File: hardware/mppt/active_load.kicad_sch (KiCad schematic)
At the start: 10 parts, among them Q601 Q_NMOS_GSD

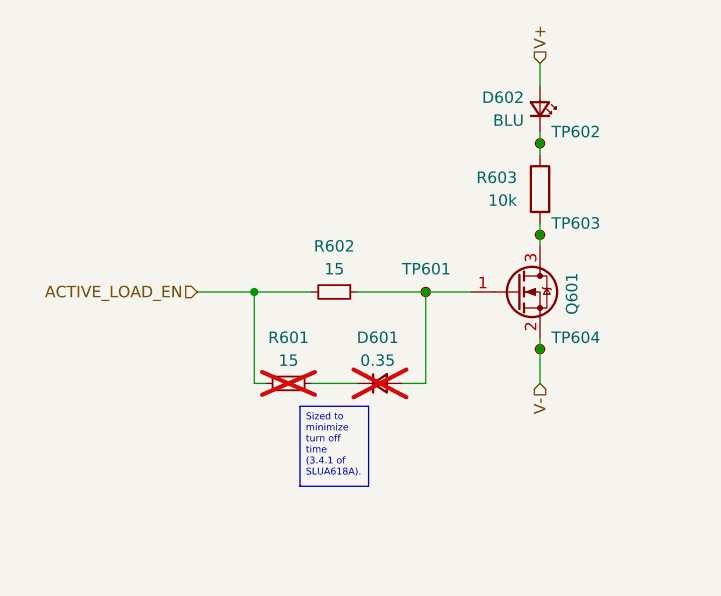
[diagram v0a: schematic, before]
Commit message: run through mppt sch, going through bom
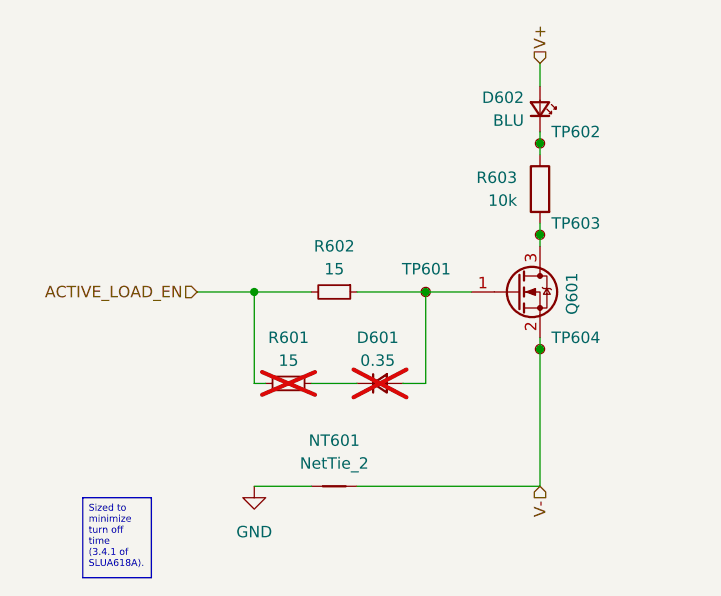
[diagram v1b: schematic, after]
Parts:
- added NT601: NetTie_2, symbol Device:NetTie_2
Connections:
- net V-: now also NT601.2
- new net GND: NT601.1

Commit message: update final missing pieces for sch, moving to bom pop
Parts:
- removed Q601: Q_NMOS_GSD, Package_TO_SOT_SMD:SOT-23-3, symbol Device:Q_NMOS_GSD
- added Q601: Q_NMOS_GDS, Package_TO_SOT_SMD:SOT-223-3_TabPin2, symbol Device:Q_NMOS_GDS
- D601: symbol Device:D_Small -> Device:D_Schottky_Small
- NT601: footprint (none) -> NetTie:NetTie-2_SMD_Pad2.0mm
- R601, R602: footprint Resistor_SMD:R_0805_2012Metric_Pad1.20x1.40mm_HandSolder -> (none)
- TP601, TP602, TP603, TP604: footprint TestPoint:TestPoint_Keystone_5000-5004_Miniature -> TestPoint:TestPoint_Pad_D1.0mm; Manufacturer Keystone Electronics -> (none); P/N 5000 -> (none)
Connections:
- net V-: now also Q601.3 (S)
- net at D601.2 (A), R602.1, TP601.1: now also Q601.1 (G)
- net at R603.2, TP603.1: now also Q601.2 (D)
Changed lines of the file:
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@@
 			)
 		)
-		(property "Footprint" ""
+		(property "Footprint" "NetTie:NetTie-2_SMD_Pad2.0mm"
 			(at 116.84 123.19 0)
 			(effects
@@
 			)
 		)
-		(property "Datasheet" "~"
+		(property "Datasheet" ""
 			(at 116.84 123.19 0)
 			(effects
@@
 			)
 		)
-		(property "Footprint" "TestPoint:TestPoint_Keystone_5000-5004_Miniature"
+		(property "Footprint" "TestPoint:TestPoint_Pad_D1.0mm"
 			(at 121.92 101.6 0)
 			(effects
@@
 			)
 		)
-		(property "Datasheet" "https://www.keyelco.com/userAssets/file/M65p56.pdf"
+		(property "Datasheet" ""
 			(at 121.92 101.6 0)
 			(effects
@@
 			)
 		)
-		(property "Manufacturer" "Keystone Electronics"
+		(property "Manufacturer" ""
 			(at 127 101.6 0)
 			(effects
@@
 			)
 		)
-		(property "P/N" "5000"
+		(property "P/N" ""
 			(at 127 101.6 0)
 			(effects
@@
 			)
 		)
-		(property "Footprint" "TestPoint:TestPoint_Keystone_5000-5004_Miniature"
+		(property "Footprint" "TestPoint:TestPoint_Pad_D1.0mm"
 			(at 144.78 107.95 0)
 			(effects
@@
 			)
 		)
-		(property "Datasheet" "https://www.keyelco.com/userAssets/file/M65p56.pdf"
+		(property "Datasheet" ""
 			(at 144.78 107.95 0)
 			(effects
@@
 			)
 		)
-		(property "Manufacturer" "Keystone Electronics"
+		(property "Manufacturer" ""
 			(at 139.7 107.95 0)
 			(effects
@@
 			)
 		)
-		(property "P/N" "5000"
+		(property "P/N" ""
 			(at 139.7 107.95 0)
 			(effects
@@
 	)
 	(symbol
-		(lib_id "Device:D_Small")
+		(lib_id "Device:D_Schottky_Small")
 		(at 121.92 111.76 0)
 		(mirror x)
@@
 			)
 		)
-		(property "Datasheet" "https://www.mouser.com/datasheet/2/115/DIOD_S_A0002960396_1-2542090.pdf"
+		(property "Datasheet" "~"
 			(at 121.92 111.76 90)
 			(effects
@@
 			)
 		)
-		(property "Description" "Diode, small symbol"
+		(property "Description" "Schottky diode, small symbol"
 			(at 121.92 111.76 0)
 			(effects
@@
 			)
 		)
-		(property "Footprint" "TestPoint:TestPoint_Keystone_5000-5004_Miniature"
+		(property "Footprint" "TestPoint:TestPoint_Pad_D1.0mm"
 			(at 144.78 85.09 0)
 			(effects
@@
 			)
 		)
-		(property "Datasheet" "https://www.keyelco.com/userAssets/file/M65p56.pdf"
+		(property "Datasheet" ""
 			(at 144.78 85.09 0)
 			(effects
@@
 			)
 		)
-		(property "Manufacturer" "Keystone Electronics"
+		(property "Manufacturer" ""
 			(at 139.7 85.09 0)
 			(effects
@@
 			)
 		)
-		(property "P/N" "5000"
+		(property "P/N" ""
 			(at 139.7 85.09 0)
 			(effects
@@
 			)
 		)
-		(property "Footprint" "TestPoint:TestPoint_Keystone_5000-5004_Miniature"
+		(property "Footprint" "TestPoint:TestPoint_Pad_D1.0mm"
 			(at 144.78 95.25 0)
 			(effects
@@
 			)
 		)
-		(property "Datasheet" "https://www.keyelco.com/userAssets/file/M65p56.pdf"
+		(property "Datasheet" ""
 			(at 144.78 95.25 0)
 			(effects
@@
 			)
 		)
-		(property "Manufacturer" "Keystone Electronics"
+		(property "Manufacturer" ""
 			(at 139.7 95.25 0)
 			(effects
@@
 			)
 		)
-		(property "P/N" "5000"
+		(property "P/N" ""
 			(at 139.7 95.25 0)
 			(effects
@@
 				(path "/83ad0d2f-976b-4ec4-beba-98e6b6988069/1e7e948a-199f-4420-b7b6-1130e9474bfe/a7b76023-5527-427b-b6b3-61ece243dcb4"
 					(reference "TP703")
-					(unit 1)
-				)
-			)
-		)
-	)
-	(symbol
-		(lib_id "Device:Q_NMOS_GSD")
-		(at 137.16 101.6 0)
-		(unit 1)
-		(exclude_from_sim no)
-		(in_bom yes)
-		(on_board yes)
-		(dnp no)
-		(property "Reference" "Q601"
-			(at 143.256 104.14 90)
-			(effects
-				(font
-					(size 1.27 1.27)
-				)
-				(justify left)
-			)
-		)
-		(property "Value" "Q_NMOS_GSD"
-			(at 143.51 102.8699 0)
-			(effects
-				(font
-					(size 1.27 1.27)
-				)
-				(justify left)
-				(hide yes)
-			)
-		)
-		(property "Footprint" "Package_TO_SOT_SMD:SOT-23-3"
-			(at 142.24 99.06 0)
-			(effects
-				(font
-					(size 1.27 1.27)
-				)
-				(hide yes)
-			)
-		)
-		(property "Datasheet" "https://www.mouser.com/datasheet/2/196/Infineon_BSS131_DS_v02_06_en-1226437.pdf"
-			(at 137.16 101.6 0)
-			(effects
-				(font
-					(size 1.27 1.27)
-				)
-				(hide yes)
-			)
-		)
-		(property "Description" "N-MOSFET transistor, gate/source/drain"
-			(at 137.16 101.6 0)
-			(effects
-				(font
-					(size 1.27 1.27)
-				)
-				(hide yes)
-			)
-		)
-		(property "Distributor" ""
-			(at 137.16 101.6 0)
-			(effects
-				(font
-					(size 1.27 1.27)
-				)
-				(hide yes)
-			)
-		)
-		(property "Manufacturer" "Infineon"
-			(at 137.16 101.6 0)
-			(effects
-				(font
-					(size 1.27 1.27)
-				)
-				(hide yes)
-			)
-		)
-		(property "P/N" "BSS131"
-			(at 137.16 101.6 0)
-			(effects
-				(font
-					(size 1.27 1.27)
-				)
-				(hide yes)
-			)
-		)
-		(property "LCSC Part #" ""
-			(at 137.16 101.6 0)
-			(effects
-				(font
-					(size 1.27 1.27)
-				)
-				(hide yes)
-			)
-		)
-		(property "Cost" ""
-			(at 137.16 101.6 0)
-			(effects
-				(font
-					(size 1.27 1.27)
-				)
-				(hide yes)
-			)
-		)
-		(property "Notes" ""
-			(at 137.16 101.6 0)
-			(effects
-				(font
-					(size 1.27 1.27)
-				)
-				(hide yes)
-			)
-		)
-		(property "Sim.Device" ""
-			(at 137.16 101.6 0)
-			(effects
-				(font
-					(size 1.27 1.27)
-				)
-				(hide yes)
-			)
-		)
-		(property "Sim.Pins" ""
-			(at 137.16 101.6 0)
-			(effects
-				(font
-					(size 1.27 1.27)
-				)
-				(hide yes)
-			)
-		)
-		(pin "3"
-		)
-		(pin "1"
-		)
-		(pin "2"
-		)
-		(instances
-			(project "mppt"
-				(path "/83ad0d2f-976b-4ec4-beba-98e6b6988069/1e7e948a-199f-4420-b7b6-1130e9474bfe/3cc71787-1ecf-4ebc-9258-dc128425d892"
-					(reference "Q601")
-					(unit 1)
-				)
-				(path "/83ad0d2f-976b-4ec4-beba-98e6b6988069/1e7e948a-199f-4420-b7b6-1130e9474bfe/a7b76023-5527-427b-b6b3-61ece243dcb4"
-					(reference "Q701")
 					(unit 1)
 				)
@@
 			)
 		)
-		(property "Footprint" "Resistor_SMD:R_0805_2012Metric_Pad1.20x1.40mm_HandSolder"
+		(property "Footprint" ""
 			(at 111.76 111.76 0)
 			(effects
@@
 	)
 	(symbol
+		(lib_id "Device:Q_NMOS_GDS")
+		(at 137.16 101.6 0)
+		(unit 1)
+		(exclude_from_sim no)
+		(in_bom yes)
+		(on_board yes)
+		(dnp no)
+		(fields_autoplaced yes)
+		(property "Reference" "Q601"
+			(at 143.51 100.3299 0)
+			(effects
+				(font
+					(size 1.27 1.27)
+				)
+				(justify left)
+			)
+		)
+		(property "Value" "Q_NMOS_GDS"
+			(at 143.51 102.8699 0)
+			(effects
+				(font
+					(size 1.27 1.27)
+				)
+				(justify left)
+			)
+		)
+		(property "Footprint" "Package_TO_SOT_SMD:SOT-223-3_TabPin2"
+			(at 142.24 99.06 0)
+			(effects
+				(font
+					(size 1.27 1.27)
+				)
+				(hide yes)
+			)
+		)
+		(property "Datasheet" "~"
+			(at 137.16 101.6 0)
+			(effects
+				(font
+					(size 1.27 1.27)
+				)
+				(hide yes)
+			)
+		)
+		(property "Description" "N-MOSFET transistor, gate/drain/source"
+			(at 137.16 101.6 0)
+			(effects
+				(font
+					(size 1.27 1.27)
+				)
+				(hide yes)
+			)
+		)
+		(property "Distributor" ""
+			(at 137.16 101.6 0)
+			(effects
+				(font
+					(size 1.27 1.27)
+				)
+				(hide yes)
+			)
+		)
+		(property "Manufacturer" "Infineon"
+			(at 137.16 101.6 0)
+			(effects
+				(font
+					(size 1.27 1.27)
+				)
+				(hide yes)
+			)
+		)
+		(property "P/N" "BSP297H6327"
+			(at 137.16 101.6 0)
+			(effects
+				(font
+					(size 1.27 1.27)
+				)
+				(hide yes)
+			)
+		)
+		(property "LCSC Part #" ""
+			(at 137.16 101.6 0)
+			(effects
+				(font
+					(size 1.27 1.27)
+				)
+				(hide yes)
+			)
+		)
+		(property "Cost" ""
+			(at 137.16 101.6 0)
+			(effects
+				(font
+					(size 1.27 1.27)
+				)
+				(hide yes)
+			)
+		)
+		(property "Notes" ""
+			(at 137.16 101.6 0)
+			(effects
+				(font
+					(size 1.27 1.27)
+				)
+				(hide yes)
+			)
+		)
+		(pin "3"
+		)
+		(pin "2"
+		)
+		(pin "1"
+		)
+		(instances
+			(project "mppt"
+				(path "/83ad0d2f-976b-4ec4-beba-98e6b6988069/1e7e948a-199f-4420-b7b6-1130e9474bfe/3cc71787-1ecf-4ebc-9258-dc128425d892"
+					(reference "Q601")
+					(unit 1)
+				)
+				(path "/83ad0d2f-976b-4ec4-beba-98e6b6988069/1e7e948a-199f-4420-b7b6-1130e9474bfe/a7b76023-5527-427b-b6b3-61ece243dcb4"
+					(reference "Q701")
+					(unit 1)
+				)
+			)
+		)
+	)
+	(symbol
 		(lib_id "Device:R_Small")
 		(at 116.84 101.6 270)
@@
 			)
 		)
-		(property "Footprint" "Resistor_SMD:R_0805_2012Metric_Pad1.20x1.40mm_HandSolder"
+		(property "Footprint" ""
 			(at 116.84 101.6 0)
 			(effects

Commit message: bom consolidated, starting layout
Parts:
- D601: value 0.35 -> Schottky
- D602: Manufacturer (none) -> Kingbright; P/N (none) -> APT2012QBC/D
- NT601: footprint NetTie:NetTie-2_SMD_Pad2.0mm -> NetTie:NetTie-2_SMD_Pad0.5mm
- R601, R602: footprint (none) -> Resistor_SMD:R_1210_3225Metric_Pad1.30x2.65mm_HandSolder; P/N (none) -> CRCW121015R0FKEA
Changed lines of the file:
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@@
 			)
 		)
-		(property "Footprint" "NetTie:NetTie-2_SMD_Pad2.0mm"
+		(property "Footprint" "NetTie:NetTie-2_SMD_Pad0.5mm"
 			(at 116.84 123.19 0)
 			(effects
@@
 		)
 		(property "Description" "Net tie, 2 pins"
-			(at 116.84 123.19 0)
-			(effects
-				(font
-					(size 1.27 1.27)
-				)
-				(hide yes)
-			)
-		)
-		(property "Sim.Device" ""
-			(at 116.84 123.19 0)
-			(effects
-				(font
-					(size 1.27 1.27)
-				)
-				(hide yes)
-			)
-		)
-		(property "Sim.Pins" ""
 			(at 116.84 123.19 0)
 			(effects
@@
 			)
 		)
-		(property "Sim.Device" ""
-			(at 127 101.6 0)
-			(effects
-				(font
-					(size 1.27 1.27)
-				)
-				(hide yes)
-			)
-		)
-		(property "Sim.Pins" ""
-			(at 127 101.6 0)
-			(effects
-				(font
-					(size 1.27 1.27)
-				)
-				(hide yes)
-			)
-		)
 		(pin "1"
 		)
@@
 			)
 		)
-		(property "Sim.Device" ""
-			(at 139.7 107.95 0)
-			(effects
-				(font
-					(size 1.27 1.27)
-				)
-				(hide yes)
-			)
-		)
-		(property "Sim.Pins" ""
-			(at 139.7 107.95 0)
-			(effects
-				(font
-					(size 1.27 1.27)
-				)
-				(hide yes)
-			)
-		)
 		(pin "1"
 		)
@@
 			)
 		)
-		(property "Value" "0.35"
+		(property "Value" "Schottky"
 			(at 121.666 109.22 0)
 			(effects
@@
 			)
 		)
-		(property "Datasheet" "~"
+		(property "Datasheet" "https://www.mouser.com/datasheet/2/115/DIOD_S_A0002960396_1-2542090.pdf"
 			(at 121.92 111.76 90)
 			(effects
@@
 		(property "Notes" ""
 			(at 121.92 111.76 90)
-			(effects
-				(font
-					(size 1.27 1.27)
-				)
-				(hide yes)
-			)
-		)
-		(property "Sim.Device" ""
-			(at 121.92 111.76 0)
-			(effects
-				(font
-					(size 1.27 1.27)
-				)
-				(hide yes)
-			)
-		)
-		(property "Sim.Pins" ""
-			(at 121.92 111.76 0)
 			(effects
 				(font
@@
 			)
 		)
-		(property "Datasheet" ""
+		(property "Datasheet" "https://www.mouser.com/datasheet/2/216/APT2012QBC_D-226241.pdf"
 			(at 139.7 81.28 90)
 			(effects
@@
 			)
 		)
-		(property "Manufacturer" ""
+		(property "Manufacturer" "Kingbright"
 			(at 139.7 81.28 90)
 			(effects
@@
 			)
 		)
-		(property "P/N" ""
+		(property "P/N" " APT2012QBC/D "
 			(at 139.7 81.28 90)
 			(effects
@@
 		(property "Notes" ""
 			(at 139.7 81.28 90)
-			(effects
-				(font
-					(size 1.27 1.27)
-				)
-				(hide yes)
-			)
-		)
-		(property "Sim.Device" ""
-			(at 139.7 81.28 0)
-			(effects
-				(font
-					(size 1.27 1.27)
-				)
-				(hide yes)
-			)
-		)
-		(property "Sim.Pins" ""
-			(at 139.7 81.28 0)
 			(effects
 				(font
@@
 			)
 		)
-		(property "Sim.Device" ""
-			(at 139.7 85.09 0)
-			(effects
-				(font
-					(size 1.27 1.27)
-				)
-				(hide yes)
-			)
-		)
-		(property "Sim.Pins" ""
-			(at 139.7 85.09 0)
-			(effects
-				(font
-					(size 1.27 1.27)
-				)
-				(hide yes)
-			)
-		)
 		(pin "1"
 		)
@@
 			)
 		)
-		(property "Sim.Device" ""
-			(at 139.7 95.25 0)
-			(effects
-				(font
-					(size 1.27 1.27)
-				)
-				(hide yes)
-			)
-		)
-		(property "Sim.Pins" ""
-			(at 139.7 95.25 0)
-			(effects
-				(font
-					(size 1.27 1.27)
-				)
-				(hide yes)
-			)
-		)
 		(pin "1"
 		)
@@
 			)
 		)
-		(property "Footprint" ""
+		(property "Footprint" "Resistor_SMD:R_1210_3225Metric_Pad1.30x2.65mm_HandSolder"
 			(at 111.76 111.76 0)
 			(effects
@@
 			)
 		)
-		(property "Datasheet" ""
+		(property "Datasheet" "https://www.vishay.com/docs/20035/dcrcwe3.pdf"
 			(at 111.76 111.76 0)
 			(effects
@@
 			)
 		)
-		(property "P/N" ""
-			(at 111.76 111.76 0)
-			(effects
-				(font
-					(size 1.27 1.27)
-				)
-				(hide yes)
-			)
-		)
-		(property "Sim.Device" ""
-			(at 111.76 111.76 0)
-			(effects
-				(font
-					(size 1.27 1.27)
-				)
-				(hide yes)
-			)
-		)
-		(property "Sim.Pins" ""
+		(property "P/N" "CRCW121015R0FKEA "
 			(at 111.76 111.76 0)
 			(effects
@@
 			)
 		)
-		(property "Sim.Device" ""
-			(at 139.7 90.17 0)
-			(effects
-				(font
-					(size 1.27 1.27)
-				)
-				(hide yes)
-			)
-		)
-		(property "Sim.Pins" ""
-			(at 139.7 90.17 0)
-			(effects
-				(font
-					(size 1.27 1.27)
-				)
-				(hide yes)
-			)
-		)
 		(pin "2"
 		)
@@
 			)
 		)
-		(property "Datasheet" "~"
+		(property "Datasheet" "https://www.mouser.com/datasheet/2/196/Infineon_BSP297_DS_v02_02_en-1226465.pdf"
 			(at 137.16 101.6 0)
 			(effects
@@
 			)
 		)
-		(property "Footprint" ""
+		(property "Footprint" "Resistor_SMD:R_1210_3225Metric_Pad1.30x2.65mm_HandSolder"
 			(at 116.84 101.6 0)
 			(effects
@@
 			)
 		)
-		(property "Datasheet" ""
+		(property "Datasheet" "https://www.vishay.com/docs/20035/dcrcwe3.pdf"
 			(at 116.84 101.6 0)
 			(effects
@@
 			)
 		)
-		(property "P/N" ""
+		(property "P/N" "CRCW121015R0FKEA "
 			(at 116.84 101.6 0)
 			(effects
-				(font
-					(size 1.27 1.27)
-				)
-				(hide yes)
-			)
-		)
-		(property "Sim.Device" ""
-			(at 116.84 101.6 0)
-			(effects
-				(font
-					(size 1.27 1.27)
-				)
-				(hide yes)
-			)
-		)
-		(property "Sim.Pins" ""
-			(at 116.84 101.6 0)
-			(effects

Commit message: PCB variant for power regulation breakout.
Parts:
- D601, R601: now left out of the parts list
- D602, Q601, R602, R603, TP601, TP602, TP603, TP604: now not fitted; now left out of the parts list
- NT601: now not fitted
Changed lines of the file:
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@@
 		(exclude_from_sim no)
 		(in_bom no)
-		(on_board yes)
-		(dnp no)
+		(on_board no)
+		(dnp yes)
 		(fields_autoplaced yes)
 		(property "Reference" "NT601"
@@
 		(unit 1)
 		(exclude_from_sim no)
-		(in_bom yes)
-		(on_board yes)
-		(dnp no)
+		(in_bom no)
+		(on_board no)
+		(dnp yes)
 		(property "Reference" "TP601"
 			(at 129.794 99.06 0)
@@
 		(unit 1)
 		(exclude_from_sim no)
-		(in_bom yes)
-		(on_board yes)
-		(dnp no)
+		(in_bom no)
+		(on_board no)
+		(dnp yes)
 		(fields_autoplaced yes)
 		(property "Reference" "TP604"
@@
 		(unit 1)
 		(exclude_from_sim no)
-		(in_bom yes)
-		(on_board yes)
+		(in_bom no)
+		(on_board no)
 		(dnp yes)
 		(property "Reference" "D601"
@@
 		(unit 1)
 		(exclude_from_sim no)
-		(in_bom yes)
-		(on_board yes)
-		(dnp no)
+		(in_bom no)
+		(on_board no)
+		(dnp yes)
 		(fields_autoplaced yes)
 		(property "Reference" "#PWR0601"
@@
 		(unit 1)
 		(exclude_from_sim no)
-		(in_bom yes)
-		(on_board yes)
-		(dnp no)
+		(in_bom no)
+		(on_board no)
+		(dnp yes)
 		(property "Reference" "D602"
 			(at 137.922 80.01 90)
@@
 		(unit 1)
 		(exclude_from_sim no)
-		(in_bom yes)
-		(on_board yes)
-		(dnp no)
+		(in_bom no)
+		(on_board no)
+		(dnp yes)
 		(fields_autoplaced yes)
 		(property "Reference" "TP602"
@@
 		(unit 1)
 		(exclude_from_sim no)
-		(in_bom yes)
-		(on_board yes)
-		(dnp no)
+		(in_bom no)
+		(on_board no)
+		(dnp yes)
 		(fields_autoplaced yes)
 		(property "Reference" "TP603"
@@
 		(unit 1)
 		(exclude_from_sim no)
-		(in_bom yes)
-		(on_board yes)
+		(in_bom no)
+		(on_board no)
 		(dnp yes)
 		(fields_autoplaced yes)
@@
 		(unit 1)
 		(exclude_from_sim no)
-		(in_bom yes)
-		(on_board yes)
-		(dnp no)
+		(in_bom no)
+		(on_board no)
+		(dnp yes)
 		(property "Reference" "R603"
 			(at 137.16 88.8999 0)
@@
 		(unit 1)
 		(exclude_from_sim no)
-		(in_bom yes)
-		(on_board yes)
-		(dnp no)
+		(in_bom no)
+		(on_board no)
+		(dnp yes)
 		(fields_autoplaced yes)
 		(property "Reference" "Q601"
@@
 		(unit 1)
 		(exclude_from_sim no)
-		(in_bom yes)
-		(on_board yes)
-		(dnp no)
+		(in_bom no)
+		(on_board no)
+		(dnp yes)
 		(fields_autoplaced yes)
 		(property "Reference" "R602"

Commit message: converter schematic and layout.
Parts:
- D601, D602, NT601, Q601, R601, R602, R603, TP601, TP602, TP603, TP604: now fitted; now in the parts list
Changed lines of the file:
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@@
 		(unit 1)
 		(exclude_from_sim no)
-		(in_bom no)
-		(on_board no)
-		(dnp yes)
+		(in_bom yes)
+		(on_board yes)
+		(dnp no)
 		(fields_autoplaced yes)
 		(property "Reference" "NT601"
@@
 		(unit 1)
 		(exclude_from_sim no)
-		(in_bom no)
-		(on_board no)
-		(dnp yes)
+		(in_bom yes)
+		(on_board yes)
+		(dnp no)
 		(property "Reference" "TP601"
 			(at 129.794 99.06 0)
@@
 		(unit 1)
 		(exclude_from_sim no)
-		(in_bom no)
-		(on_board no)
-		(dnp yes)
+		(in_bom yes)
+		(on_board yes)
+		(dnp no)
 		(fields_autoplaced yes)
 		(property "Reference" "TP604"
@@
 		(unit 1)
 		(exclude_from_sim no)
-		(in_bom no)
-		(on_board no)
-		(dnp yes)
+		(in_bom yes)
+		(on_board yes)
+		(dnp no)
 		(property "Reference" "D601"
 			(at 121.666 106.68 0)
@@
 		(unit 1)
 		(exclude_from_sim no)
-		(in_bom no)
-		(on_board no)
-		(dnp yes)
+		(in_bom yes)
+		(on_board yes)
+		(dnp no)
 		(fields_autoplaced yes)
 		(property "Reference" "#PWR0601"
@@
 		(unit 1)
 		(exclude_from_sim no)
-		(in_bom no)
-		(on_board no)
-		(dnp yes)
+		(in_bom yes)
+		(on_board yes)
+		(dnp no)
 		(property "Reference" "D602"
 			(at 137.922 80.01 90)
@@
 		(unit 1)
 		(exclude_from_sim no)
-		(in_bom no)
-		(on_board no)
-		(dnp yes)
+		(in_bom yes)
+		(on_board yes)
+		(dnp no)
 		(fields_autoplaced yes)
 		(property "Reference" "TP602"
@@
 		(unit 1)
 		(exclude_from_sim no)
-		(in_bom no)
-		(on_board no)
-		(dnp yes)
+		(in_bom yes)
+		(on_board yes)
+		(dnp no)
 		(fields_autoplaced yes)
 		(property "Reference" "TP603"
@@
 		(unit 1)
 		(exclude_from_sim no)
-		(in_bom no)
-		(on_board no)
-		(dnp yes)
+		(in_bom yes)
+		(on_board yes)
+		(dnp no)
 		(fields_autoplaced yes)
 		(property "Reference" "R601"
@@
 		(unit 1)
 		(exclude_from_sim no)
-		(in_bom no)
-		(on_board no)
-		(dnp yes)
+		(in_bom yes)
+		(on_board yes)
+		(dnp no)
 		(property "Reference" "R603"
 			(at 137.16 88.8999 0)
@@
 		(unit 1)
 		(exclude_from_sim no)
-		(in_bom no)
-		(on_board no)
-		(dnp yes)
+		(in_bom yes)
+		(on_board yes)
+		(dnp no)
 		(fields_autoplaced yes)
 		(property "Reference" "Q601"
@@
 		(unit 1)
 		(exclude_from_sim no)
-		(in_bom no)
-		(on_board no)
-		(dnp yes)
+		(in_bom yes)
+		(on_board yes)
+		(dnp no)
 		(fields_autoplaced yes)
 		(property "Reference" "R602"

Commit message: remove testpoints, integrat 60% of layout
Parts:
- removed TP601, TP602, TP603, TP604: TestPoint_Small, TestPoint:TestPoint_Pad_D1.0mm, symbol Connector:TestPoint_Small
- R601, R602: footprint Resistor_SMD:R_1210_3225Metric_Pad1.30x2.65mm_HandSolder -> Resistor_SMD:R_0603_1608Metric; P/N CRCW121015R0FKEA -> CRCW060315R0FKEAHP
